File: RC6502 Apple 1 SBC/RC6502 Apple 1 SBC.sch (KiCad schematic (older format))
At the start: 43 parts, among them J1 VP GND, J2 Arduino Nano, J3 Backplane, J4 Hole, J5 Hole, J6 Hole, J7 Hole, J8 Power, SW1 RESET, U1 WD65C02, U2 HM62256BLP-7, U3 74HCT138, U4 28C256, U5 74HCT00, U6 NE555, U7 74HCT04, U8 WD65C21, U9 MCP23S17, X1 1MHz

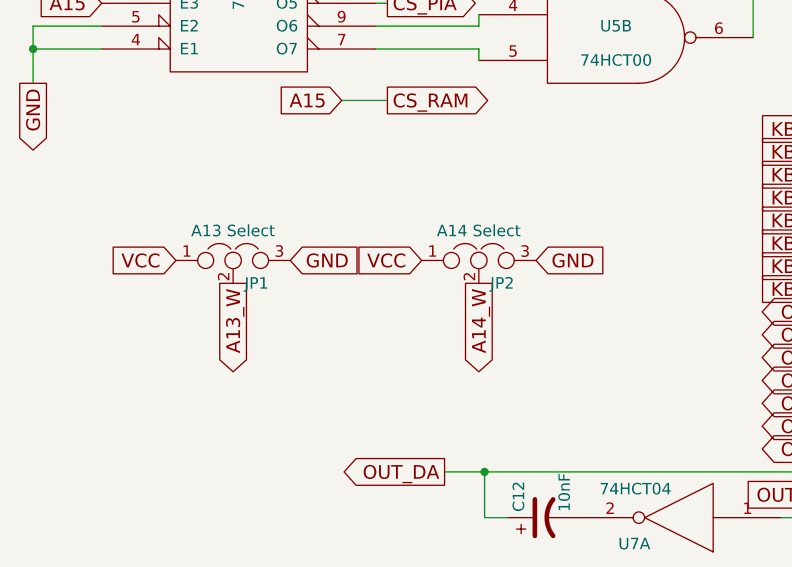
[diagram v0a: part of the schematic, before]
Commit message: Added ROM reference to SBC
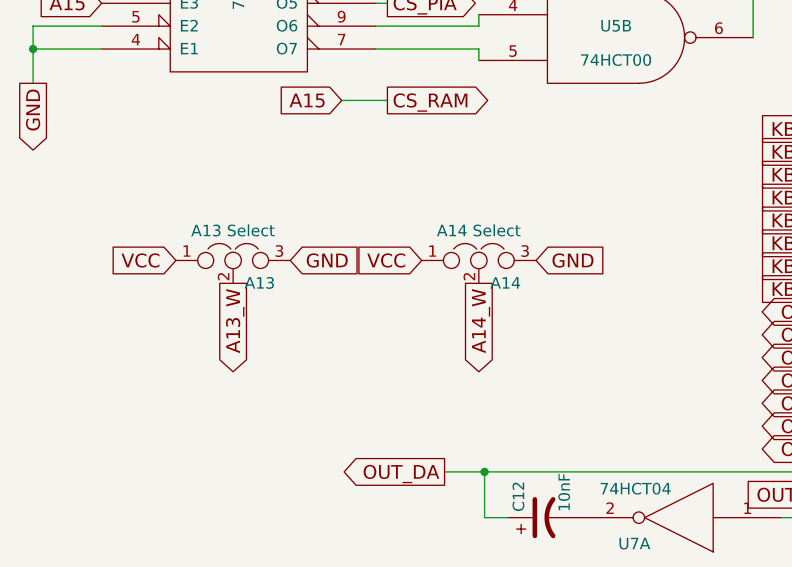
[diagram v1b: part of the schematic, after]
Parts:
- renumbered JP1 to A13, JP2 to A14
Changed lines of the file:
@@
 $EndComp
 $Comp
-L Jumper_NC_Dual JP1
+L Jumper_NC_Dual A13
 U 1 1 5941C8BC
 P 1475 2350
-F 0 "JP1" H 1525 2250 50  0000 L CNN
+F 0 "A13" H 1525 2250 50  0000 L CNN
 F 1 "A13 Select" H 1475 2450 50  0000 C BNN
 F 2 "Pin_Headers:Pin_Header_Straight_1x03_Pitch2.54mm" H 1475 2350 50  0001 C CNN
@@
 $EndComp
 $Comp
-L Jumper_NC_Dual JP2
+L Jumper_NC_Dual A14
 U 1 1 5941C8BD
 P 2550 2350
-F 0 "JP2" H 2600 2250 50  0000 L CNN
+F 0 "A14" H 2600 2250 50  0000 L CNN
 F 1 "A14 Select" H 2550 2450 50  0000 C BNN
 F 2 "Pin_Headers:Pin_Header_Straight_1x03_Pitch2.54mm" H 2550 2350 50  0001 C CNN

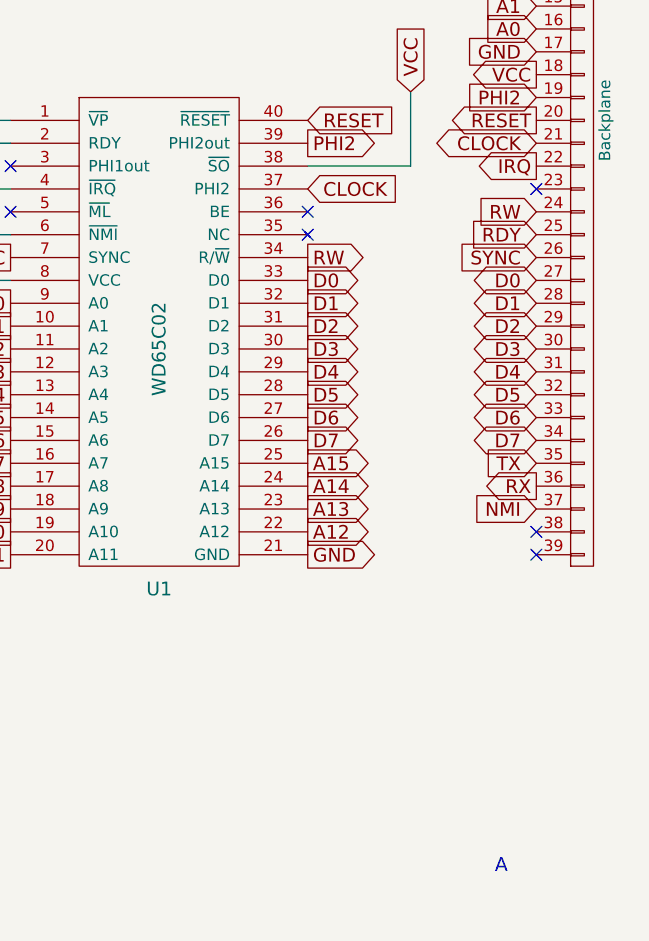
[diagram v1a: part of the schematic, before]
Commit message: SBC Revision B
Revision A still don't work with W65c02 processors, added BE signal pull-up (untested wether this improves 65c02 compatibility).
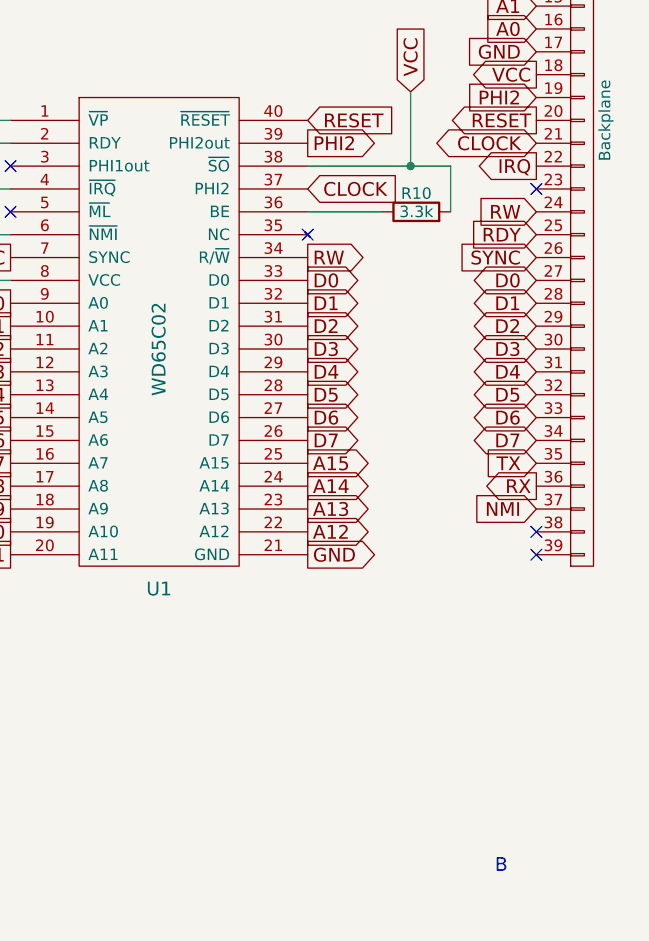
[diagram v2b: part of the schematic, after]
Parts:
- added R10: 3.3k, Resistors_THT:R_Axial_DIN0207_L6.3mm_D2.5mm_P10.16mm_Horizontal, symbol R
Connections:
- net VCC: now also R10.2
- net at U1.36 (BE): now also R10.1
- no-connect marks 43 -> 42
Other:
- note added: "B"
- note removed: "A"
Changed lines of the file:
@@
 RC6502 Apple 1 SBC
 Text Notes 10650 7650 2    60   ~ 0
-A
+B
 Text GLabel 5525 2875 2    60   BiDi ~ 0
 D5
@@
 D6
 NoConn ~ 9775 4850
-NoConn ~ 9775 4750
 NoConn ~ 8475 4750
 Text GLabel 9775 4650 2    60   Input ~ 0
@@
 	10225 4225 10225 4550
 Wire Wire Line
-	10225 4550 9775 4550
+	9775 4550 10400 4550
 Wire Wire Line
 	7500 4850 8475 4850
@@
 Wire Wire Line
 	10550 2025 10450 2025
+$Comp
+L R R10
+U 1 1 596284F8
+P 10250 4750
+F 0 "R10" V 10330 4750 50  0000 C CNN
+F 1 "3.3k" V 10250 4750 50  0000 C CNN
+F 2 "Resistors_THT:R_Axial_DIN0207_L6.3mm_D2.5mm_P10.16mm_Horizontal" V 10180 4750 50  0001 C CNN
+F 3 "" H 10250 4750 50  0001 C CNN
+	1    10250 4750
+	0    -1   -1   0
+$EndComp
+Wire Wire Line
+	10100 4750 9775 4750
+Wire Wire Line
+	10400 4550 10400 4750
+Connection ~ 10225 4550
 $EndSCHEMATC

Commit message: SBC uses new oscillator footprint
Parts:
- X1: footprint Oscillators:Oscillator_DIP-14 -> Oscillator:Oscillator_DIP-14
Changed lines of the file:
@@
 LIBS:valves
 LIBS:65xx
+LIBS:rc6502_backplane
 LIBS:RC6502 Apple 1 SBC-cache
 EELAYER 25 0
@@
 F 0 "X1" H 550 6850 50  0000 L CNN
 F 1 "1MHz" H 800 6350 50  0000 L CNN
-F 2 "Oscillators:Oscillator_DIP-14" H 1200 6250 50  0001 C CNN
+F 2 "Oscillator:Oscillator_DIP-14" H 1200 6250 50  0001 C CNN
 F 3 "" H 650 6600 50  0001 C CNN
 	1    750  6600

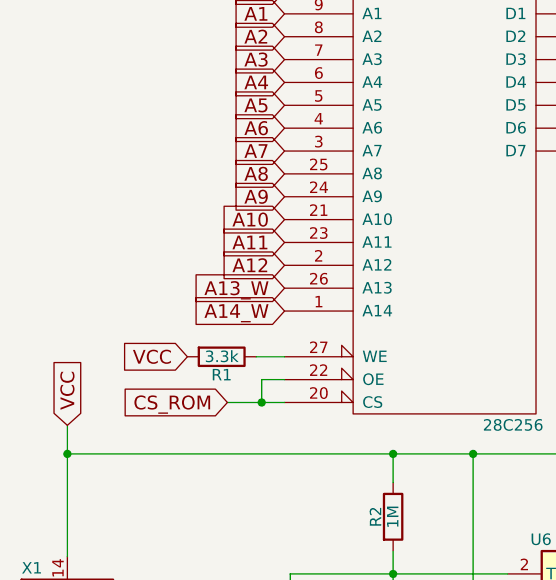
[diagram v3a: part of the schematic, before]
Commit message: Added ROM enable jumper to SBC
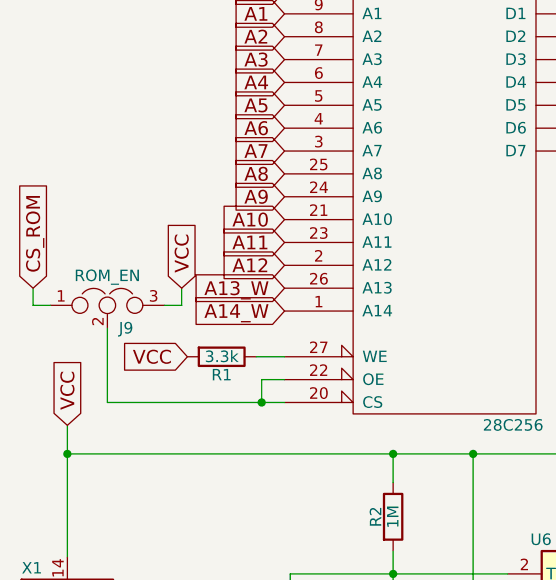
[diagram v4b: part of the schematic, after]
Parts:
- added J9: ROM_EN, Pin_Headers:Pin_Header_Straight_1x03_Pitch2.54mm, symbol Jumper_NC_Dual
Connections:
- net CS_ROM: now also J9.1; no longer U4.20 (CS), U4.22 (OE)
- net VCC: now also J9.3
- new net: J9.2, U4.20 (CS), U4.22 (OE)
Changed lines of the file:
@@
 	1600 5525 1600 5625
 Wire Wire Line
-	1450 5625 1700 5625
+	925  5625 1700 5625
 Connection ~ 1600 5625
 $Comp
@@
 Wire Wire Line
 	2100 1225 2150 1225
-Text GLabel 1450 5625 0    60   Input ~ 0
+Text GLabel 600  5125 1    60   Input ~ 0
 CS_ROM
 $Comp
@@
 	10400 4550 10400 4750
 Connection ~ 10225 4550
+$Comp
+L Jumper_NC_Dual J9
+U 1 1 5C3B495B
+P 925 5200
+F 0 "J9" H 975 5100 50  0000 L CNN
+F 1 "ROM_EN" H 925 5300 50  0000 C BNN
+F 2 "Pin_Headers:Pin_Header_Straight_1x03_Pitch2.54mm" H 925 5200 50  0001 C CNN
+F 3 "" H 925 5200 50  0001 C CNN
+	1    925  5200
+	1    0    0    -1
+$EndComp
+Wire Wire Line
+	675  5200 600  5200
+Wire Wire Line
+	600  5200 600  5125
+Wire Wire Line
+	925  5300 925  5625
+Text GLabel 1250 5125 1    60   Input ~ 0
+VCC
+Wire Wire Line
+	1250 5125 1250 5200
+Wire Wire Line
+	1250 5200 1175 5200
 $EndSCHEMATC

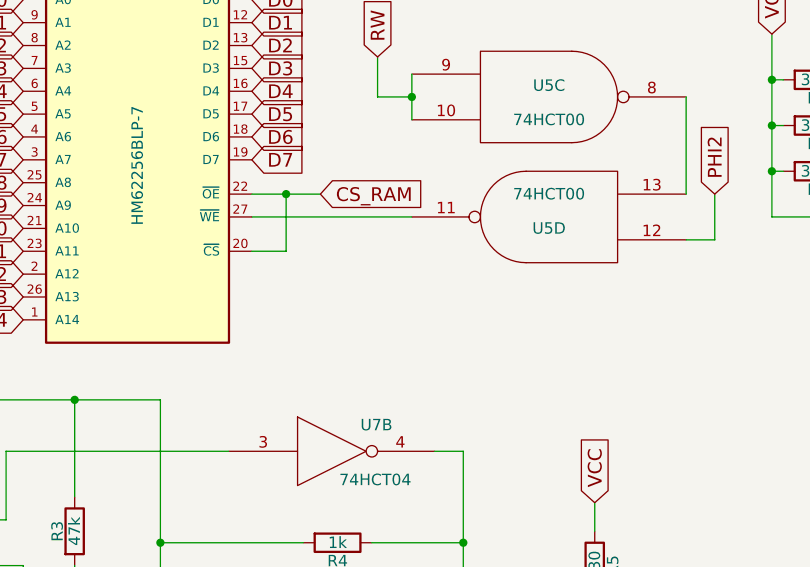
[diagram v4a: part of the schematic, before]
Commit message: Added RAM enable jumper to SBC
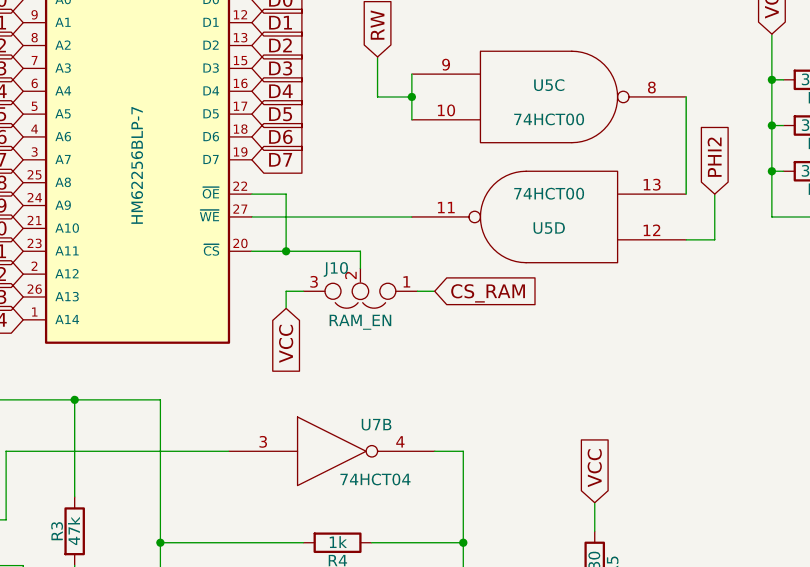
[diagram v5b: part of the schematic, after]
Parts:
- added J10: RAM_EN, Pin_Headers:Pin_Header_Straight_1x03_Pitch2.54mm, symbol Jumper_NC_Dual
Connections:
- net A15: now also J10.1; no longer U2.20 (~CS), U2.22 (~OE)
- net VCC: now also J10.3
- new net: J10.2, U2.20 (~CS), U2.22 (~OE)
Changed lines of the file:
@@
 A0
 Wire Wire Line
-	4875 4950 5175 4950
-Wire Wire Line
-	5025 4950 5025 5200
-Wire Wire Line
-	5025 5200 4875 5200
-Connection ~ 5025 4950
+	4875 5200 5350 5200
 Text GLabel 9775 4450 2    60   Output ~ 0
 PHI2
@@
 Wire Wire Line
 	1950 1650 2150 1650
-Text GLabel 5175 4950 2    60   Input ~ 0
+Text GLabel 5675 5375 2    60   Input ~ 0
 CS_RAM
 Wire Wire Line
@@
 Wire Wire Line
 	1250 5200 1175 5200
+$Comp
+L Jumper_NC_Dual J10
+U 1 1 5C3B8C28
+P 5350 5375
+F 0 "J10" H 5400 5275 50  0000 L CNN
+F 1 "RAM_EN" H 5350 5475 50  0000 C BNN
+F 2 "Pin_Headers:Pin_Header_Straight_1x03_Pitch2.54mm" H 5350 5375 50  0001 C CNN
+F 3 "" H 5350 5375 50  0001 C CNN
+	1    5350 5375
+	-1   0    0    1
+$EndComp
+Wire Wire Line
+	5600 5375 5675 5375
+Text GLabel 5025 5450 3    60   Input ~ 0
+VCC
+Wire Wire Line
+	5025 5450 5025 5375
+Wire Wire Line
+	5025 5375 5100 5375
+Wire Wire Line
+	5350 5200 5350 5275
+Connection ~ 5025 5200
+Wire Wire Line
+	4875 4950 5025 4950
+Wire Wire Line
+	5025 4950 5025 5200
 $EndSCHEMATC

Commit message: Changed schematic symbol for capacitor on serial output line
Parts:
- C12: symbol CP1 -> C
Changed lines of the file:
@@
 A4
 $Comp
-L CP1 C12
+L C C12
 U 1 1 594126D2
 P 2825 3475

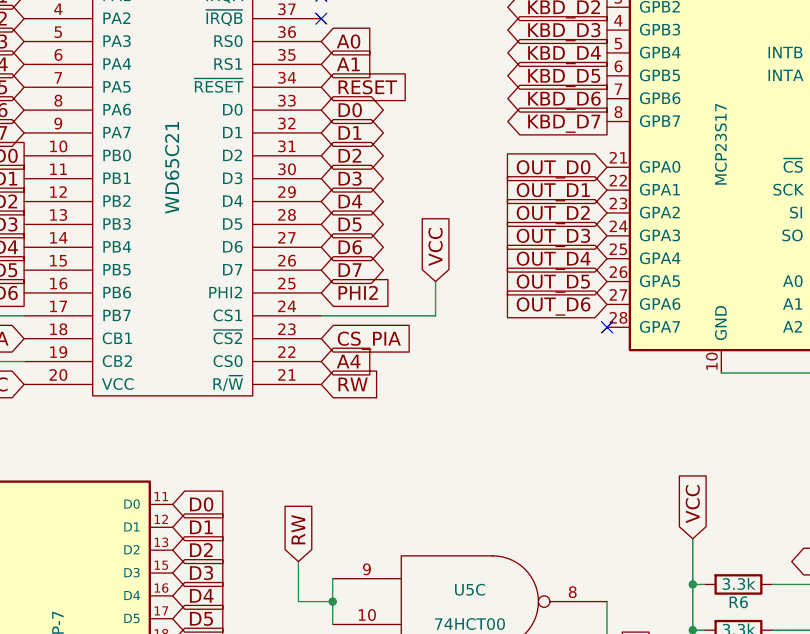
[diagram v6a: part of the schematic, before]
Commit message: Added PIA enable jumper to SBC
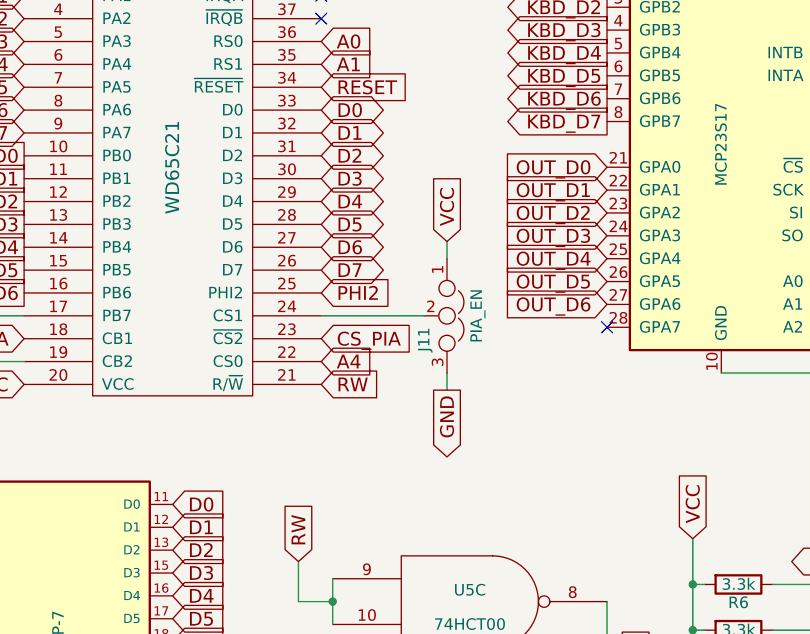
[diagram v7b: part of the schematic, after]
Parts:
- added J11: PIA_EN, Pin_Headers:Pin_Header_Straight_1x03_Pitch2.54mm, symbol Jumper_NC_Dual
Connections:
- net GND: now also J11.3
- net VCC: now also J11.1; no longer U8.24 (CS1)
- new net: J11.2, U8.24 (CS1)
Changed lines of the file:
@@
 Text GLabel 4225 1675 0    60   Output ~ 0
 GND
-Text GLabel 6025 3125 1    60   Input ~ 0
+Text GLabel 6075 2950 1    60   Input ~ 0
 VCC
 Text GLabel 5525 3475 2    60   Input ~ 0
@@
 	900  1425 600  1425
 Connection ~ 600  1425
-Wire Wire Line
-	6025 3125 6025 3275
-Wire Wire Line
-	6025 3275 5525 3275
 Wire Wire Line
 	3875 3475 4225 3475
@@
 Wire Wire Line
 	5025 4950 5025 5200
+$Comp
+L Jumper_NC_Dual J11
+U 1 1 5C5FEAD4
+P 6075 3275
+F 0 "J11" H 6125 3175 50  0000 L CNN
+F 1 "PIA_EN" H 6075 3375 50  0000 C BNN
+F 2 "Pin_Headers:Pin_Header_Straight_1x03_Pitch2.54mm" H 6075 3275 50  0001 C CNN
+F 3 "" H 6075 3275 50  0001 C CNN
+	1    6075 3275
+	0    1    1    0
+$EndComp
+Wire Wire Line
+	5525 3275 5975 3275
+Wire Wire Line
+	6075 2950 6075 3025
+Text GLabel 6075 3600 3    60   Output ~ 0
+GND
+Wire Wire Line
+	6075 3600 6075 3525
 $EndSCHEMATC

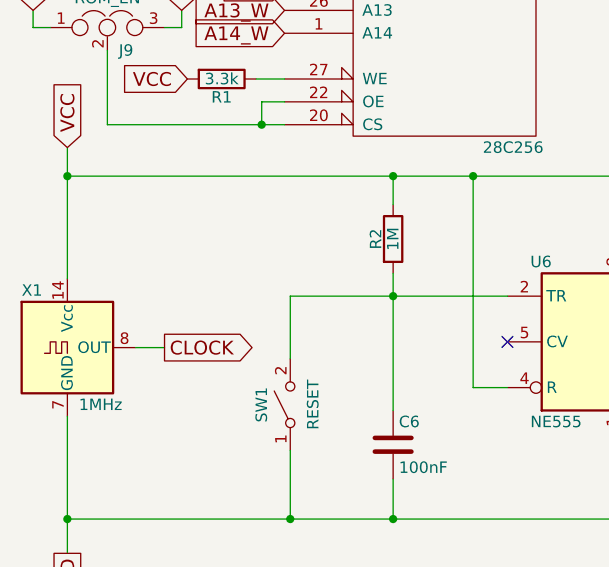
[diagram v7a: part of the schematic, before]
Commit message: Added oscillator enable jumper to SBC
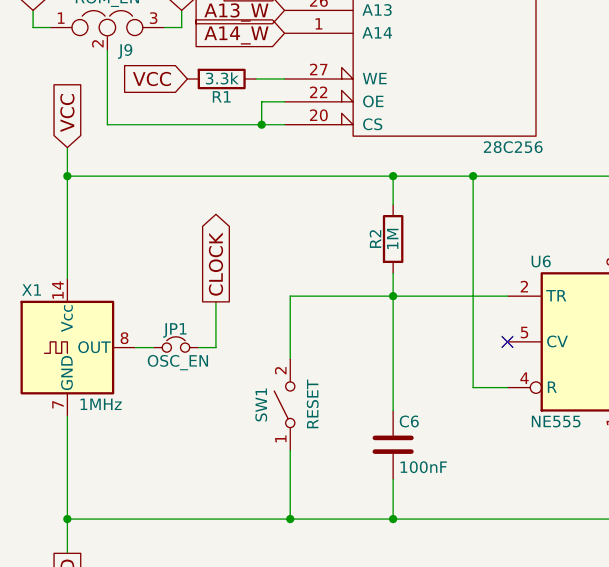
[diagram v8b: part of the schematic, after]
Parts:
- added JP1: OSC_EN, Pin_Headers:Pin_Header_Straight_1x02_Pitch2.54mm, symbol Jumper_NC_Small
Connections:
- net CLOCK: now also JP1.2; no longer X1.8 (OUT)
- new net: JP1.1, X1.8 (OUT)
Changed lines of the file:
@@
 	1    0    0    -1
 $EndComp
-Text GLabel 1175 6600 2    60   Output ~ 0
+Text GLabel 1400 6400 1    60   Output ~ 0
 CLOCK
 $Comp
@@
 Wire Wire Line
 	750  5725 750  6300
-Wire Wire Line
-	1050 6600 1175 6600
 $Comp
 L R R5
@@
 Wire Wire Line
 	6075 3600 6075 3525
+$Comp
+L Jumper_NC_Small JP1
+U 1 1 5C60279D
+P 1225 6600
+F 0 "JP1" H 1225 6680 50  0000 C CNN
+F 1 "OSC_EN" H 1235 6540 50  0000 C CNN
+F 2 "Pin_Headers:Pin_Header_Straight_1x02_Pitch2.54mm" H 1225 6600 50  0001 C CNN
+F 3 "" H 1225 6600 50  0001 C CNN
+	1    1225 6600
+	1    0    0    -1
+$EndComp
+Wire Wire Line
+	1050 6600 1125 6600
+Wire Wire Line
+	1400 6400 1400 6600
+Wire Wire Line
+	1400 6600 1325 6600
 $EndSCHEMATC
